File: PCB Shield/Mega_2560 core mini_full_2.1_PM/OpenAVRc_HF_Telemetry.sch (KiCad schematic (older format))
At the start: 10 parts, among them P18 Ecolage, P19 Module_TX, P20 TTL/RS232, P7 SPIX, U1 74LVC1G3157GV, U2 TLP290, U3 TLP290

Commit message: Update pcb files v2.1
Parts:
- added R18: 200, Resistors_SMD:R_1206, symbol R-RESCUE-Mega_2560_core_mini_full_2.0
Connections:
- net Master_PPMout: now also R18.2; no longer P19.4 (P4)
- new net: P19.4 (P4), R18.1
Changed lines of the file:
@@
 Sheet 4 7
 Title "Shield Mega2560 core Full"
-Date "2018-01-30"
+Date "2018-01-31"
 Rev "2.10"
 Comp "© Team OpenAVRc"
@@
 $EndComp
 $Comp
-L GND-RESCUE-Mega_2560_core_mini_full_2.0 #PWR066
+L GND-RESCUE-Mega_2560_core_mini_full_2.0 #PWR66
 U 1 1 59C6B422
 P 1850 5200
-F 0 "#PWR066" H 1850 4950 50  0001 C CNN
+F 0 "#PWR66" H 1850 4950 50  0001 C CNN
 F 1 "GND" H 1850 5050 50  0000 C CNN
 F 2 "" H 1850 5200 50  0000 C CNN
@@
 $EndComp
 $Comp
-L +BATT #PWR067
+L +BATT #PWR65
 U 1 1 59C6B429
 P 1600 4100
-F 0 "#PWR067" H 1600 3950 50  0001 C CNN
+F 0 "#PWR65" H 1600 3950 50  0001 C CNN
 F 1 "+BATT" H 1600 4240 50  0000 C CNN
 F 2 "" H 1600 4100 50  0000 C CNN
@@
 $EndComp
 $Comp
-L GND-RESCUE-Mega_2560_core_mini_full_2.0 #PWR068
+L GND-RESCUE-Mega_2560_core_mini_full_2.0 #PWR70
 U 1 1 59C6B436
 P 3850 2000
-F 0 "#PWR068" H 3850 1750 50  0001 C CNN
+F 0 "#PWR70" H 3850 1750 50  0001 C CNN
 F 1 "GND" V 3850 1800 50  0000 C CNN
 F 2 "" H 3850 2000 50  0000 C CNN
@@
 	1    0    0    -1
 $EndComp
-Text Label 3750 2550 1    60   ~ 0
+Text Label 3750 3050 1    60   ~ 0
 Master_PPMout
 $Comp
-L VCC #PWR069
+L VCC #PWR71
 U 1 1 59C6B43D
 P 3950 2000
-F 0 "#PWR069" H 3950 1850 50  0001 C CNN
+F 0 "#PWR71" H 3950 1850 50  0001 C CNN
 F 1 "VCC" V 3950 2200 50  0000 C CNN
 F 2 "" H 3950 2000 50  0000 C CNN
@@
 Isolation Module TTL
 $Comp
-L +BATT #PWR070
+L +BATT #PWR67
 U 1 1 59C6B445
 P 3450 2000
-F 0 "#PWR070" H 3450 1850 50  0001 C CNN
+F 0 "#PWR67" H 3450 1850 50  0001 C CNN
 F 1 "+BATT" H 3450 2140 50  0000 C CNN
 F 2 "" H 3450 2000 50  0000 C CNN
@@
 $EndComp
 $Comp
-L GND-RESCUE-Mega_2560_core_mini_full_2.0 #PWR071
+L GND-RESCUE-Mega_2560_core_mini_full_2.0 #PWR78
 U 1 1 59C6B464
 P 9650 5100
-F 0 "#PWR071" H 9650 4850 50  0001 C CNN
+F 0 "#PWR78" H 9650 4850 50  0001 C CNN
 F 1 "GND" H 9650 4950 50  0000 C CNN
 F 2 "" H 9650 5100 50  0000 C CNN
@@
 $EndComp
 $Comp
-L GND-RESCUE-Mega_2560_core_mini_full_2.0 #PWR072
+L GND-RESCUE-Mega_2560_core_mini_full_2.0 #PWR69
 U 1 1 59C6B478
 P 3750 5000
-F 0 "#PWR072" H 3750 4750 50  0001 C CNN
+F 0 "#PWR69" H 3750 4750 50  0001 C CNN
 F 1 "GND" H 3750 4850 50  0000 C CNN
 F 2 "" H 3750 5000 50  0000 C CNN
@@
 $EndComp
 $Comp
-L VCC #PWR073
+L VCC #PWR68
 U 1 1 59C6B47E
 P 3700 4200
-F 0 "#PWR073" H 3700 4050 50  0001 C CNN
+F 0 "#PWR68" H 3700 4050 50  0001 C CNN
 F 1 "VCC" H 3700 4350 50  0000 C CNN
 F 2 "" H 3700 4200 50  0000 C CNN
@@
 Text Label 3200 4250 0    60   ~ 0
 RX_module
-Text Label 4150 2550 1    60   ~ 0
+Text Label 4150 3050 1    60   ~ 0
 RX_module
-Text Label 4050 2550 1    60   ~ 0
+Text Label 4050 3050 1    60   ~ 0
 TX_module
 $Comp
@@
 $EndComp
 $Comp
-L VCC #PWR074
+L VCC #PWR77
 U 1 1 59C6B497
 P 8800 4500
-F 0 "#PWR074" H 8800 4350 50  0001 C CNN
+F 0 "#PWR77" H 8800 4350 50  0001 C CNN
 F 1 "VCC" H 8800 4650 50  0000 C CNN
 F 2 "" H 8800 4500 50  0000 C CNN
@@
 $EndComp
 $Comp
-L GND-RESCUE-Mega_2560_core_mini_full_2.0 #PWR075
+L GND-RESCUE-Mega_2560_core_mini_full_2.0 #PWR75
 U 1 1 59C6B49D
 P 7350 4500
-F 0 "#PWR075" H 7350 4250 50  0001 C CNN
+F 0 "#PWR75" H 7350 4250 50  0001 C CNN
 F 1 "GND" H 7350 4350 50  0000 C CNN
 F 2 "" H 7350 4500 50  0000 C CNN
@@
 	1950 4500 1850 4500
 Wire Wire Line
-	3750 1900 3750 2550
+	3750 2400 3750 3050
 Wire Wire Line
 	1600 4200 1600 4100
@@
 	2550 5000 2600 5000
 Wire Wire Line
-	4150 1900 4150 2550
-Wire Wire Line
-	4050 1900 4050 2550
+	4150 1900 4150 3050
+Wire Wire Line
+	4050 1900 4050 3050
 Wire Wire Line
 	3750 4550 3800 4550
@@
 	3550 1500 3550 1700
 Wire Notes Line
-	4350 1200 4350 3050
-Wire Notes Line
 	4350 1200 3200 1200
-Wire Notes Line
-	3200 1200 3200 3050
 Wire Wire Line
 	3700 4850 3800 4850
@@
 $EndComp
 $Comp
-L GND-RESCUE-Mega_2560_core_mini_full_2.0 #PWR076
+L GND-RESCUE-Mega_2560_core_mini_full_2.0 #PWR76
 U 1 1 59C6C686
 P 7550 2200
-F 0 "#PWR076" H 7550 1950 50  0001 C CNN
+F 0 "#PWR76" H 7550 1950 50  0001 C CNN
 F 1 "GND" H 7550 2050 50  0000 C CNN
 F 2 "" H 7550 2200 50  0000 C CNN
@@
 $EndComp
 $Comp
-L GND-RESCUE-Mega_2560_core_mini_full_2.0 #PWR077
+L GND-RESCUE-Mega_2560_core_mini_full_2.0 #PWR73
 U 1 1 59C6C68C
 P 7250 1850
-F 0 "#PWR077" H 7250 1600 50  0001 C CNN
+F 0 "#PWR73" H 7250 1600 50  0001 C CNN
 F 1 "GND" H 7250 1700 50  0000 C CNN
 F 2 "" H 7250 1850 50  0000 C CNN
@@
 $EndComp
 $Comp
-L VCC #PWR078
+L VCC #PWR74
 U 1 1 59C6C694
 P 7350 2000
-F 0 "#PWR078" H 7350 1850 50  0001 C CNN
+F 0 "#PWR74" H 7350 1850 50  0001 C CNN
 F 1 "VCC" V 7350 2150 50  0000 C CNN
 F 2 "" H 7350 2000 50  0000 C CNN
@@
 Sim_control
 $Comp
-L +3,3V #PWR079
+L +3,3V #PWR72
 U 1 1 59CA7757
 P 7050 1950
-F 0 "#PWR079" H 7050 1910 30  0001 C CNN
+F 0 "#PWR72" H 7050 1910 30  0001 C CNN
 F 1 "+3,3V" V 7050 2150 39  0000 C CNN
 F 2 "" H 7050 1950 60  0001 C CNN
@@
 Wire Notes Line
 	6250 3100 6250 1250
-Wire Notes Line
-	3200 3050 4350 3050
 Wire Wire Line
 	7050 4800 7600 4800
+$Comp
+L R-RESCUE-Mega_2560_core_mini_full_2.0 R18
+U 1 1 5A718C98
+P 3750 2250
+F 0 "R18" V 3650 2250 50  0000 C CNN
+F 1 "200" V 3750 2250 50  0000 C CNN
+F 2 "Resistors_SMD:R_1206" V 3680 2250 50  0001 C CNN
+F 3 "" H 3750 2250 50  0000 C CNN
+	1    3750 2250
+	1    0    0    -1
+$EndComp
+Wire Wire Line
+	3750 2100 3750 1900
+Wire Notes Line
+	3200 3150 4350 3150
+Wire Notes Line
+	4350 3150 4350 1200
+Wire Notes Line
+	3200 1200 3200 3150
 $EndSCHEMATC

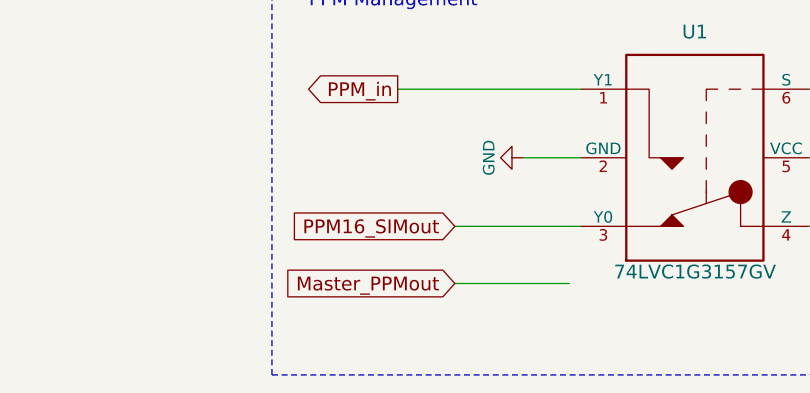
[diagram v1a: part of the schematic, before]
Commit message: Update pcb files
Remove Master_PPMout in telemetry page
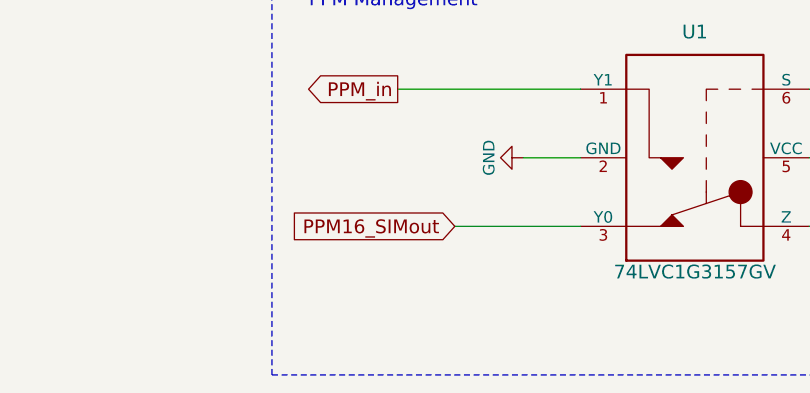
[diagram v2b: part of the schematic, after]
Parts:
- P7: footprint Pin_Header_Straight_2x05_Pitch2.54mm -> Pin_Headers:Pin_Header_Straight_2x05_Pitch2.54mm
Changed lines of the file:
@@
 LIBS:valves
 LIBS:OPEN_EVO
+LIBS:Mega_2560 core mini_full_2.1
 LIBS:Mega_2560 core mini_full_2.1-cache
 EELAYER 25 0
@@
 $EndComp
 $Comp
-L GND-RESCUE-Mega_2560_core_mini_full_2.0 #PWR66
+L GND-RESCUE-Mega_2560_core_mini_full_2.0 #PWR067
 U 1 1 59C6B422
 P 1850 5200
-F 0 "#PWR66" H 1850 4950 50  0001 C CNN
+F 0 "#PWR067" H 1850 4950 50  0001 C CNN
 F 1 "GND" H 1850 5050 50  0000 C CNN
 F 2 "" H 1850 5200 50  0000 C CNN
@@
 $EndComp
 $Comp
-L +BATT #PWR65
+L +BATT #PWR068
 U 1 1 59C6B429
 P 1600 4100
-F 0 "#PWR65" H 1600 3950 50  0001 C CNN
+F 0 "#PWR068" H 1600 3950 50  0001 C CNN
 F 1 "+BATT" H 1600 4240 50  0000 C CNN
 F 2 "" H 1600 4100 50  0000 C CNN
@@
 $EndComp
 $Comp
-L GND-RESCUE-Mega_2560_core_mini_full_2.0 #PWR70
+L GND-RESCUE-Mega_2560_core_mini_full_2.0 #PWR069
 U 1 1 59C6B436
 P 3850 2000
-F 0 "#PWR70" H 3850 1750 50  0001 C CNN
+F 0 "#PWR069" H 3850 1750 50  0001 C CNN
 F 1 "GND" V 3850 1800 50  0000 C CNN
 F 2 "" H 3850 2000 50  0000 C CNN
@@
 Master_PPMout
 $Comp
-L VCC #PWR71
+L VCC #PWR070
 U 1 1 59C6B43D
 P 3950 2000
-F 0 "#PWR71" H 3950 1850 50  0001 C CNN
+F 0 "#PWR070" H 3950 1850 50  0001 C CNN
 F 1 "VCC" V 3950 2200 50  0000 C CNN
 F 2 "" H 3950 2000 50  0000 C CNN
@@
 Isolation Module TTL
 $Comp
-L +BATT #PWR67
+L +BATT #PWR071
 U 1 1 59C6B445
 P 3450 2000
-F 0 "#PWR67" H 3450 1850 50  0001 C CNN
+F 0 "#PWR071" H 3450 1850 50  0001 C CNN
 F 1 "+BATT" H 3450 2140 50  0000 C CNN
 F 2 "" H 3450 2000 50  0000 C CNN
@@
 $EndComp
 $Comp
-L GND-RESCUE-Mega_2560_core_mini_full_2.0 #PWR78
+L GND-RESCUE-Mega_2560_core_mini_full_2.0 #PWR072
 U 1 1 59C6B464
 P 9650 5100
-F 0 "#PWR78" H 9650 4850 50  0001 C CNN
+F 0 "#PWR072" H 9650 4850 50  0001 C CNN
 F 1 "GND" H 9650 4950 50  0000 C CNN
 F 2 "" H 9650 5100 50  0000 C CNN
@@
 $EndComp
 $Comp
-L GND-RESCUE-Mega_2560_core_mini_full_2.0 #PWR69
+L GND-RESCUE-Mega_2560_core_mini_full_2.0 #PWR073
 U 1 1 59C6B478
 P 3750 5000
-F 0 "#PWR69" H 3750 4750 50  0001 C CNN
+F 0 "#PWR073" H 3750 4750 50  0001 C CNN
 F 1 "GND" H 3750 4850 50  0000 C CNN
 F 2 "" H 3750 5000 50  0000 C CNN
@@
 $EndComp
 $Comp
-L VCC #PWR68
+L VCC #PWR074
 U 1 1 59C6B47E
 P 3700 4200
-F 0 "#PWR68" H 3700 4050 50  0001 C CNN
+F 0 "#PWR074" H 3700 4050 50  0001 C CNN
 F 1 "VCC" H 3700 4350 50  0000 C CNN
 F 2 "" H 3700 4200 50  0000 C CNN
@@
 $EndComp
 $Comp
-L VCC #PWR77
+L VCC #PWR075
 U 1 1 59C6B497
 P 8800 4500
-F 0 "#PWR77" H 8800 4350 50  0001 C CNN
+F 0 "#PWR075" H 8800 4350 50  0001 C CNN
 F 1 "VCC" H 8800 4650 50  0000 C CNN
 F 2 "" H 8800 4500 50  0000 C CNN
@@
 $EndComp
 $Comp
-L GND-RESCUE-Mega_2560_core_mini_full_2.0 #PWR75
+L GND-RESCUE-Mega_2560_core_mini_full_2.0 #PWR076
 U 1 1 59C6B49D
 P 7350 4500
-F 0 "#PWR75" H 7350 4250 50  0001 C CNN
+F 0 "#PWR076" H 7350 4250 50  0001 C CNN
 F 1 "GND" H 7350 4350 50  0000 C CNN
 F 2 "" H 7350 4500 50  0000 C CNN
@@
 Wire Wire Line
 	6800 4200 7600 4200
-Wire Wire Line
-	7050 5050 7550 5050
 Wire Notes Line
 	6250 3700 10250 3700
@@
 $EndComp
 $Comp
-L GND-RESCUE-Mega_2560_core_mini_full_2.0 #PWR76
+L GND-RESCUE-Mega_2560_core_mini_full_2.0 #PWR077
 U 1 1 59C6C686
 P 7550 2200
-F 0 "#PWR76" H 7550 1950 50  0001 C CNN
+F 0 "#PWR077" H 7550 1950 50  0001 C CNN
 F 1 "GND" H 7550 2050 50  0000 C CNN
 F 2 "" H 7550 2200 50  0000 C CNN
@@
 $EndComp
 $Comp
-L GND-RESCUE-Mega_2560_core_mini_full_2.0 #PWR73
+L GND-RESCUE-Mega_2560_core_mini_full_2.0 #PWR078
 U 1 1 59C6C68C
 P 7250 1850
-F 0 "#PWR73" H 7250 1600 50  0001 C CNN
+F 0 "#PWR078" H 7250 1600 50  0001 C CNN
 F 1 "GND" H 7250 1700 50  0000 C CNN
 F 2 "" H 7250 1850 50  0000 C CNN
@@
 $EndComp
 $Comp
-L VCC #PWR74
+L VCC #PWR079
 U 1 1 59C6C694
 P 7350 2000
-F 0 "#PWR74" H 7350 1850 50  0001 C CNN
+F 0 "#PWR079" H 7350 1850 50  0001 C CNN
 F 1 "VCC" V 7350 2150 50  0000 C CNN
 F 2 "" H 7350 2000 50  0000 C CNN
@@
 F 0 "P7" H 6900 2100 50  0000 C CNN
 F 1 "SPIX" V 6900 950 50  0000 C CNN
-F 2 "Pin_Header_Straight_2x05_Pitch2.54mm" H 6900 1550 50  0001 C CNN
+F 2 "Pin_Headers:Pin_Header_Straight_2x05_Pitch2.54mm" H 6900 1550 50  0001 C CNN
 F 3 "" H 6900 1550 50  0000 C CNN
 	1    6900 1550
@@
 Text GLabel 7050 4800 0    60   Input ~ 0
 PPM16_SIMout
-Text GLabel 7050 5050 0    60   Input ~ 0
-Master_PPMout
 Text GLabel 9150 4200 2    60   Input ~ 0
 Sim_control
 $Comp
-L +3,3V #PWR72
+L +3,3V #PWR080
 U 1 1 59CA7757
 P 7050 1950
-F 0 "#PWR72" H 7050 1910 30  0001 C CNN
+F 0 "#PWR080" H 7050 1910 30  0001 C CNN
 F 1 "+3,3V" V 7050 2150 39  0000 C CNN
 F 2 "" H 7050 1950 60  0001 C CNN

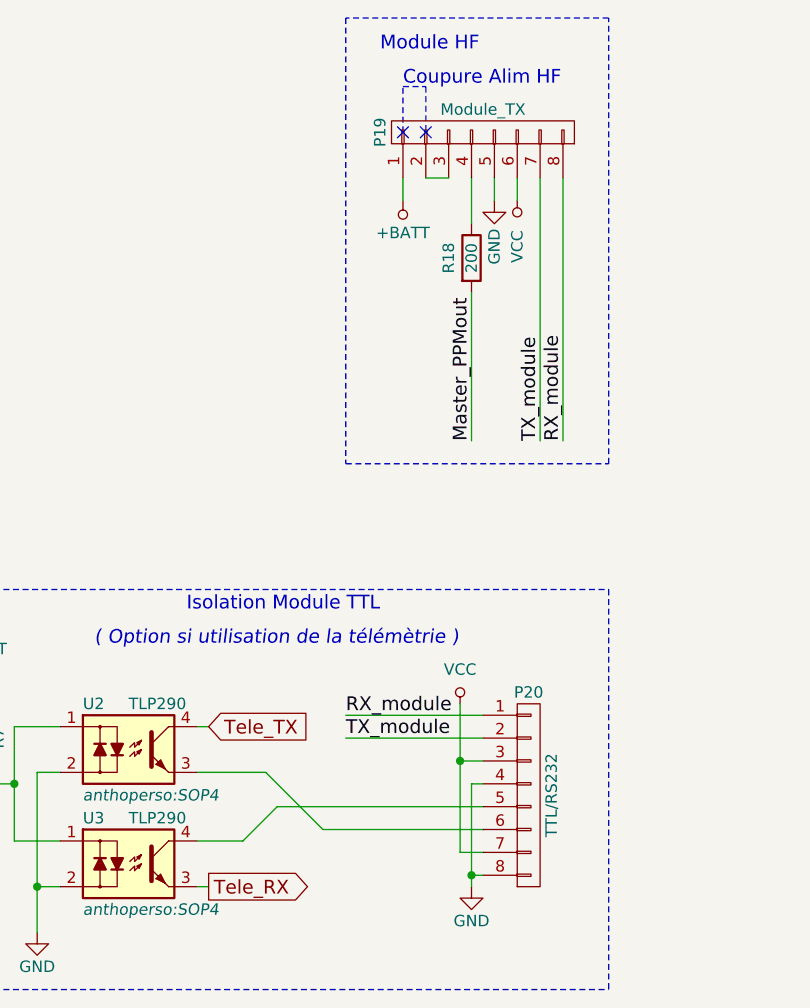
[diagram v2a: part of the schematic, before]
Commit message: Update pcb files v2.1
Add resistor 220 ohms on signal Tele_RX
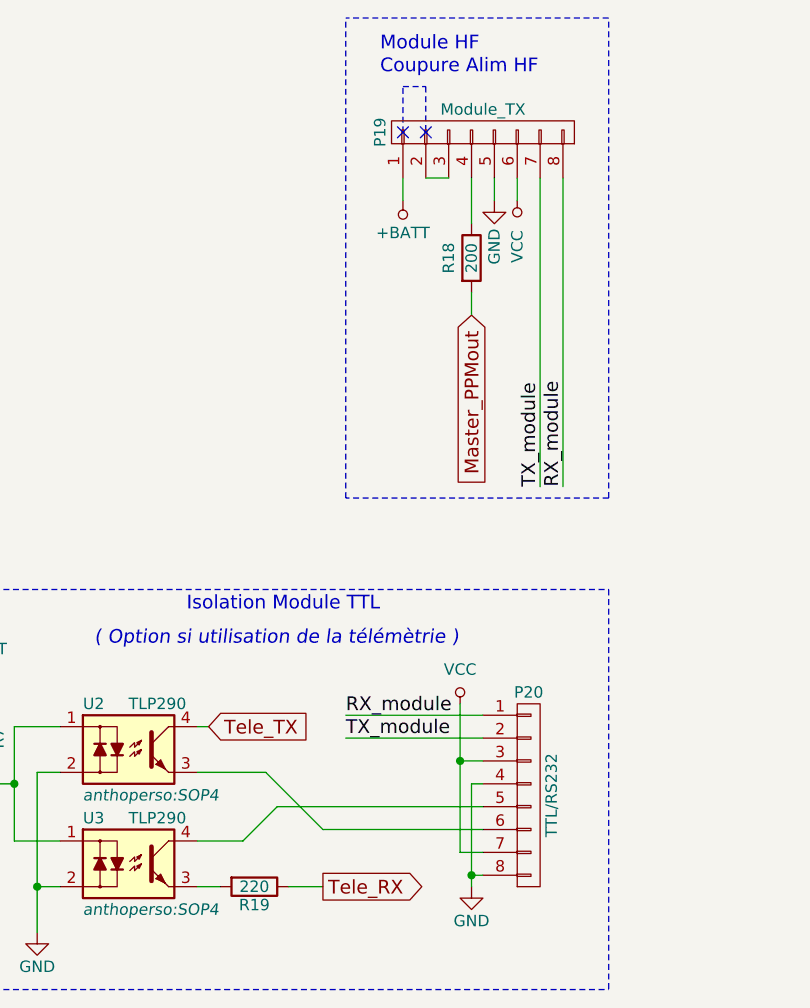
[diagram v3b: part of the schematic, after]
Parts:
- added R19: 220, Resistors_SMD:R_1206, symbol R-RESCUE-Mega_2560_core_mini_full_2.0
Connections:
- net Tele_RX: now also R19.1; no longer U3.3
- new net: R19.2, U3.3
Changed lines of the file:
@@
 Sheet 4 7
 Title "Shield Mega2560 core Full"
-Date "2018-01-31"
+Date "2018-02-03"
 Rev "2.10"
 Comp "© Team OpenAVRc"
@@
 $EndComp
 $Comp
-L GND-RESCUE-Mega_2560_core_mini_full_2.0 #PWR067
+L GND-RESCUE-Mega_2560_core_mini_full_2.0 #PWR66
 U 1 1 59C6B422
 P 1850 5200
-F 0 "#PWR067" H 1850 4950 50  0001 C CNN
+F 0 "#PWR66" H 1850 4950 50  0001 C CNN
 F 1 "GND" H 1850 5050 50  0000 C CNN
 F 2 "" H 1850 5200 50  0000 C CNN
@@
 $EndComp
 $Comp
-L +BATT #PWR068
+L +BATT #PWR65
 U 1 1 59C6B429
 P 1600 4100
-F 0 "#PWR068" H 1600 3950 50  0001 C CNN
+F 0 "#PWR65" H 1600 3950 50  0001 C CNN
 F 1 "+BATT" H 1600 4240 50  0000 C CNN
 F 2 "" H 1600 4100 50  0000 C CNN
@@
 $EndComp
 $Comp
-L GND-RESCUE-Mega_2560_core_mini_full_2.0 #PWR069
+L GND-RESCUE-Mega_2560_core_mini_full_2.0 #PWR70
 U 1 1 59C6B436
 P 3850 2000
-F 0 "#PWR069" H 3850 1750 50  0001 C CNN
+F 0 "#PWR70" H 3850 1750 50  0001 C CNN
 F 1 "GND" V 3850 1800 50  0000 C CNN
 F 2 "" H 3850 2000 50  0000 C CNN
@@
 	1    0    0    -1
 $EndComp
-Text Label 3750 3050 1    60   ~ 0
-Master_PPMout
-$Comp
-L VCC #PWR070
+$Comp
+L VCC #PWR71
 U 1 1 59C6B43D
 P 3950 2000
-F 0 "#PWR070" H 3950 1850 50  0001 C CNN
+F 0 "#PWR71" H 3950 1850 50  0001 C CNN
 F 1 "VCC" V 3950 2200 50  0000 C CNN
 F 2 "" H 3950 2000 50  0000 C CNN
@@
 Isolation Module TTL
 $Comp
-L +BATT #PWR071
+L +BATT #PWR67
 U 1 1 59C6B445
 P 3450 2000
-F 0 "#PWR071" H 3450 1850 50  0001 C CNN
+F 0 "#PWR67" H 3450 1850 50  0001 C CNN
 F 1 "+BATT" H 3450 2140 50  0000 C CNN
 F 2 "" H 3450 2000 50  0000 C CNN
@@
 $EndComp
 $Comp
-L GND-RESCUE-Mega_2560_core_mini_full_2.0 #PWR072
+L GND-RESCUE-Mega_2560_core_mini_full_2.0 #PWR78
 U 1 1 59C6B464
 P 9650 5100
-F 0 "#PWR072" H 9650 4850 50  0001 C CNN
+F 0 "#PWR78" H 9650 4850 50  0001 C CNN
 F 1 "GND" H 9650 4950 50  0000 C CNN
 F 2 "" H 9650 5100 50  0000 C CNN
@@
 $EndComp
 $Comp
-L GND-RESCUE-Mega_2560_core_mini_full_2.0 #PWR073
+L GND-RESCUE-Mega_2560_core_mini_full_2.0 #PWR69
 U 1 1 59C6B478
 P 3750 5000
-F 0 "#PWR073" H 3750 4750 50  0001 C CNN
+F 0 "#PWR69" H 3750 4750 50  0001 C CNN
 F 1 "GND" H 3750 4850 50  0000 C CNN
 F 2 "" H 3750 5000 50  0000 C CNN
@@
 $EndComp
 $Comp
-L VCC #PWR074
+L VCC #PWR68
 U 1 1 59C6B47E
 P 3700 4200
-F 0 "#PWR074" H 3700 4050 50  0001 C CNN
+F 0 "#PWR68" H 3700 4050 50  0001 C CNN
 F 1 "VCC" H 3700 4350 50  0000 C CNN
 F 2 "" H 3700 4200 50  0000 C CNN
@@
 	1    0    0    -1
 $EndComp
-Text Notes 3450 1500 0    60   ~ 0
+Text Notes 3350 1450 0    60   ~ 0
 Coupure Alim HF
 Text Label 3200 4350 0    60   ~ 0
@@
 Text Label 3200 4250 0    60   ~ 0
 RX_module
-Text Label 4150 3050 1    60   ~ 0
+Text Label 4150 3250 1    60   ~ 0
 RX_module
-Text Label 4050 3050 1    60   ~ 0
+Text Label 4050 3250 1    60   ~ 0
 TX_module
 $Comp
@@
 $EndComp
 $Comp
-L VCC #PWR075
+L VCC #PWR77
 U 1 1 59C6B497
 P 8800 4500
-F 0 "#PWR075" H 8800 4350 50  0001 C CNN
+F 0 "#PWR77" H 8800 4350 50  0001 C CNN
 F 1 "VCC" H 8800 4650 50  0000 C CNN
 F 2 "" H 8800 4500 50  0000 C CNN
@@
 $EndComp
 $Comp
-L GND-RESCUE-Mega_2560_core_mini_full_2.0 #PWR076
+L GND-RESCUE-Mega_2560_core_mini_full_2.0 #PWR75
 U 1 1 59C6B49D
 P 7350 4500
-F 0 "#PWR076" H 7350 4250 50  0001 C CNN
+F 0 "#PWR75" H 7350 4250 50  0001 C CNN
 F 1 "GND" H 7350 4350 50  0000 C CNN
 F 2 "" H 7350 4500 50  0000 C CNN
@@
 	1950 4500 1850 4500
 Wire Wire Line
-	3750 2400 3750 3050
-Wire Wire Line
 	1600 4200 1600 4100
 Wire Wire Line
 	2600 4300 2550 4300
 Wire Wire Line
-	2550 5000 2600 5000
-Wire Wire Line
-	4150 1900 4150 3050
-Wire Wire Line
-	4050 1900 4050 3050
+	4150 1900 4150 3250
+Wire Wire Line
+	4050 1900 4050 3250
 Wire Wire Line
 	3750 4550 3800 4550
@@
 $EndComp
 $Comp
-L GND-RESCUE-Mega_2560_core_mini_full_2.0 #PWR077
+L GND-RESCUE-Mega_2560_core_mini_full_2.0 #PWR76
 U 1 1 59C6C686
 P 7550 2200
-F 0 "#PWR077" H 7550 1950 50  0001 C CNN
+F 0 "#PWR76" H 7550 1950 50  0001 C CNN
 F 1 "GND" H 7550 2050 50  0000 C CNN
 F 2 "" H 7550 2200 50  0000 C CNN
@@
 $EndComp
 $Comp
-L GND-RESCUE-Mega_2560_core_mini_full_2.0 #PWR078
+L GND-RESCUE-Mega_2560_core_mini_full_2.0 #PWR73
 U 1 1 59C6C68C
 P 7250 1850
-F 0 "#PWR078" H 7250 1600 50  0001 C CNN
+F 0 "#PWR73" H 7250 1600 50  0001 C CNN
 F 1 "GND" H 7250 1700 50  0000 C CNN
 F 2 "" H 7250 1850 50  0000 C CNN
@@
 $EndComp
 $Comp
-L VCC #PWR079
+L VCC #PWR74
 U 1 1 59C6C694
 P 7350 2000
-F 0 "#PWR079" H 7350 1850 50  0001 C CNN
+F 0 "#PWR74" H 7350 1850 50  0001 C CNN
 F 1 "VCC" V 7350 2150 50  0000 C CNN
 F 2 "" H 7350 2000 50  0000 C CNN
@@
 Wire Notes Line
 	6250 5450 6250 3700
-Text GLabel 2600 5000 2    60   Output ~ 0
+Text GLabel 3100 5000 2    60   Output ~ 0
 Tele_RX
 Text GLabel 2600 4300 2    60   Input ~ 0
@@
 Sim_control
 $Comp
-L +3,3V #PWR080
+L +3,3V #PWR72
 U 1 1 59CA7757
 P 7050 1950
-F 0 "#PWR080" H 7050 1910 30  0001 C CNN
+F 0 "#PWR72" H 7050 1910 30  0001 C CNN
 F 1 "+3,3V" V 7050 2150 39  0000 C CNN
 F 2 "" H 7050 1950 60  0001 C CNN
@@
 Wire Wire Line
 	3750 2100 3750 1900
-Wire Notes Line
-	3200 3150 4350 3150
-Wire Notes Line
-	4350 3150 4350 1200
-Wire Notes Line
-	3200 1200 3200 3150
+$Comp
+L R-RESCUE-Mega_2560_core_mini_full_2.0 R19
+U 1 1 5A757DEE
+P 2800 5000
+F 0 "R19" V 2880 5000 50  0000 C CNN
+F 1 "220" V 2800 5000 50  0000 C CNN
+F 2 "Resistors_SMD:R_1206" V 2730 5000 50  0001 C CNN
+F 3 "" H 2800 5000 50  0000 C CNN
+	1    2800 5000
+	0    1    1    0
+$EndComp
+Wire Wire Line
+	3100 5000 2950 5000
+Wire Wire Line
+	2650 5000 2550 5000
+Text GLabel 3750 2500 3    60   Input ~ 0
+Master_PPMout
+Wire Wire Line
+	3750 2500 3750 2400
+Wire Notes Line
+	4350 3300 3200 3300
+Wire Notes Line
+	4350 3300 4350 1200
+Wire Notes Line
+	3200 3300 3200 1200
 $EndSCHEMATC
